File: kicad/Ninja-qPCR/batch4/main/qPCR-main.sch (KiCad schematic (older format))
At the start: 39 parts, among them J1 Raspberry_Pi_3A_Plus_wpi, J2 Conn_01x03_Male, J3 Conn_01x01_Male, J4 Conn_01x01_Male, J5 Conn_02x03_Odd_Even, J6 Conn_02x03_Odd_Even, J7 Conn_02x03_Odd_Even, Q1 Q_NMOS_GSD, Q2 Q_NMOS_GSD, Q3 Q_NMOS_GSD, Q4 Q_NMOS_GSD, Q5 Q_NMOS_GSD, Q6 Q_NMOS_GSD, SW1 TACTILE_4

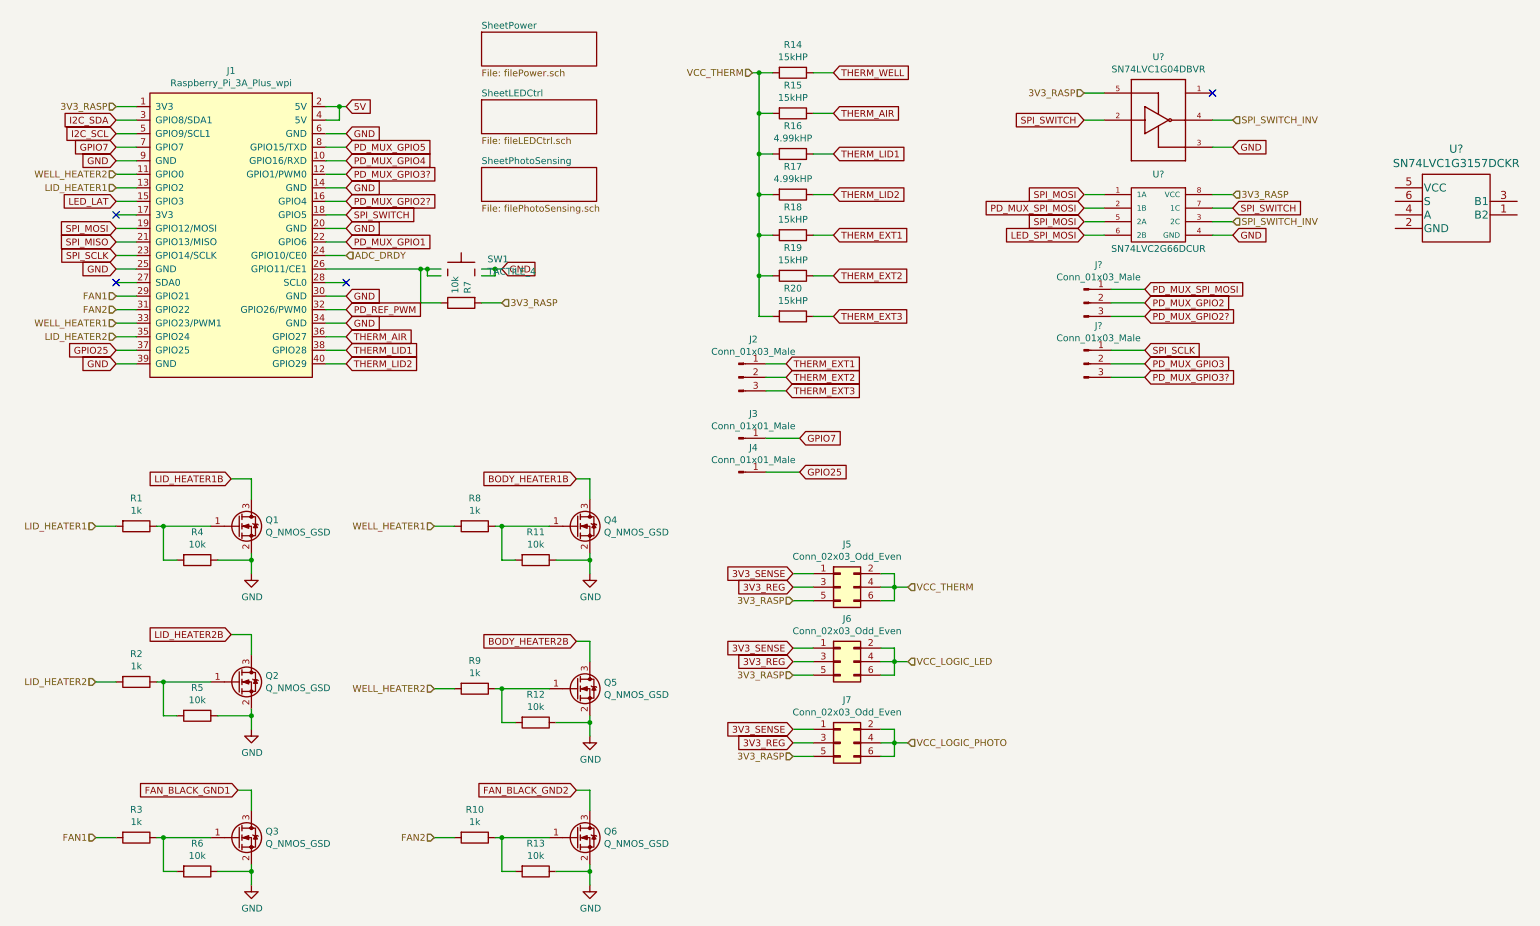
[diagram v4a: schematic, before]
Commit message: add gg component yaml
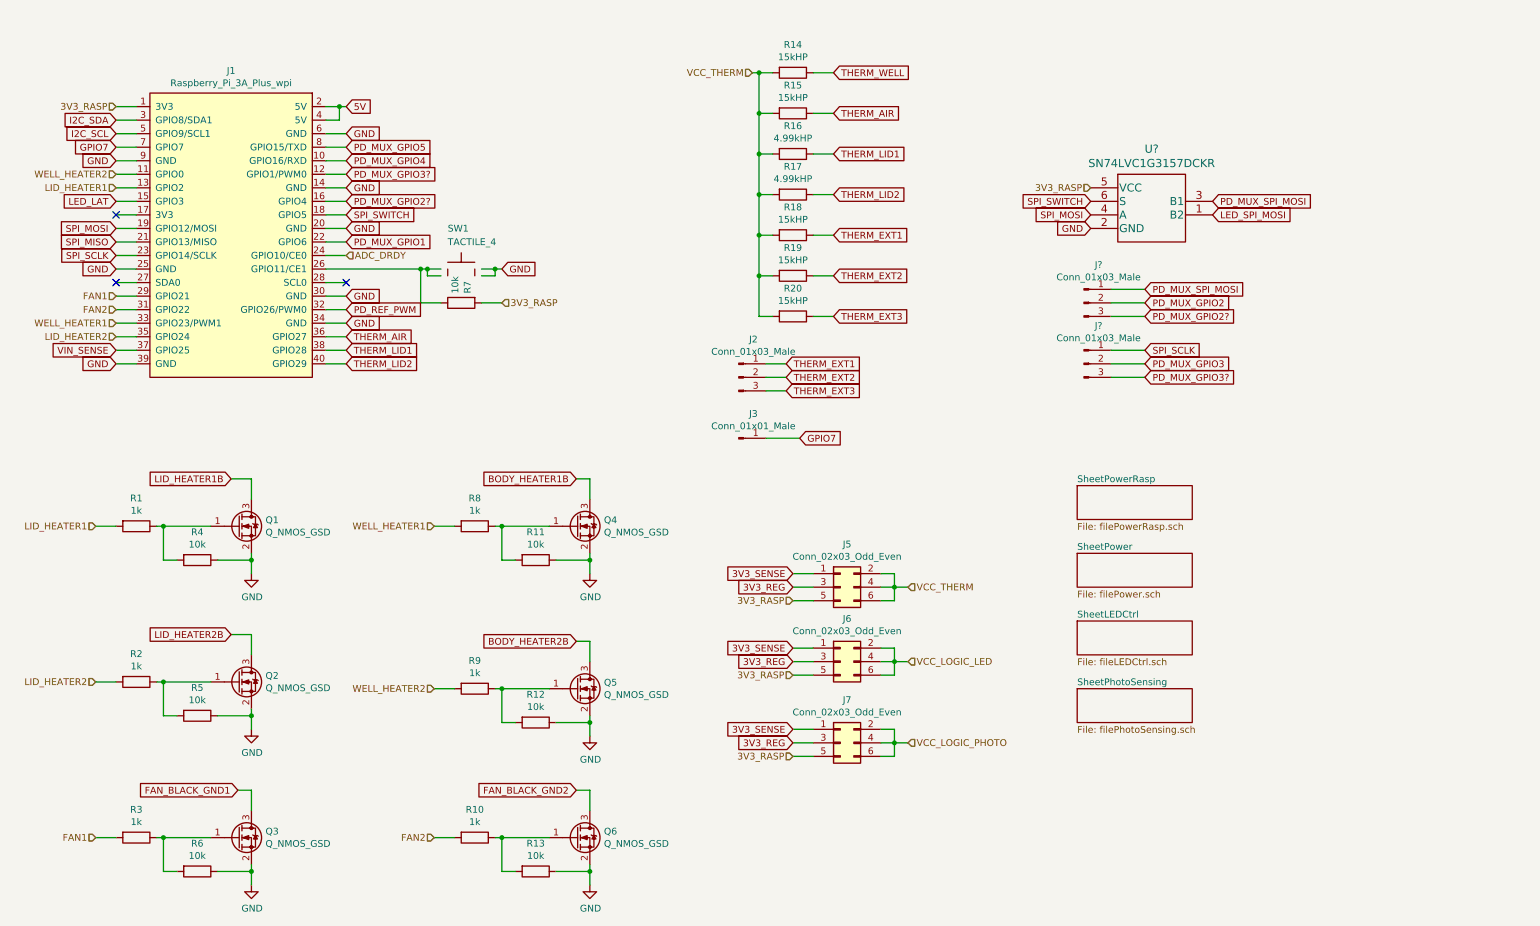
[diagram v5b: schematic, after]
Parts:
- removed J4: Conn_01x01_Male, Pin_Headers:Pin_Header_Straight_1x01_Pitch2.54mm, symbol Connector:Conn_01x01_Male
- removed U?: SN74LVC1G04DBVR, Ninja-qPCR:SN74LVC1G04DBVR, symbol Ninja-qPCR:SN74LVC1G04DBVR
- removed U?: SN74LVC2G66DCUR, Ninja-qPCR:SN74LVC2G66DCUR, symbol Ninja-qPCR:SN74LVC2G66DCUR
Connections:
- net 3V3_RASP: now also U?.5 (VCC)
- net GND: now also U?.2 (GND)
- net LED_SPI_MOSI: now also U?.1 (B2)
- net PD_MUX_SPI_MOSI: now also U?.3 (B1)
- net SPI_MOSI: now also U?.4 (A)
- net SPI_SWITCH: now also U?.6 (S)
- net GPIO25 renamed VIN_SENSE
- no-connect marks 4 -> 3
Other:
- moved on the sheet: U?
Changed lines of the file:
@@
 $Descr A4 11693 8268
 encoding utf-8
-Sheet 1 4
+Sheet 1 5
 Title ""
 Date ""
@@
 Wire Wire Line
 	3700 2950 3550 2950
-Text GLabel 2000 3250 0    50   Input ~ 0
-GPIO25
 Wire Wire Line
 	2000 3250 2150 3250
@@
 	4850 2900 4700 2900
 Wire Wire Line
-	4850 2650 4800 2650
-Text GLabel 4850 2650 2    50   Input ~ 0
-GND
-Wire Wire Line
 	4300 2700 4300 2650
 Connection ~ 4300 2650
@@
 Connection ~ 4800 2650
 $Sheet
-S 4700 900  850  250
+S 9100 4750 850  250
 U 5F7093B5
 F0 "SheetPower" 50
@@
 Text GLabel 7050 3900 2    50   Input ~ 0
 GPIO7
-Text GLabel 7050 4150 2    50   Input ~ 0
-GPIO25
 Wire Wire Line
 	7050 3900 6800 3900
-Wire Wire Line
-	7050 4150 6800 4150
 NoConn ~ 2000 2250
 Wire Wire Line
@@
 Wire Wire Line
 	9600 3450 9350 3450
-Text GLabel 9150 1550 0    50   Input ~ 0
-SPI_SWITCH
-NoConn ~ 10100 1350
-Text HLabel 10250 1550 2    50   Input ~ 0
-SPI_SWITCH_INV
-Text GLabel 10250 1750 2    50   Input ~ 0
-GND
-Wire Wire Line
-	10250 1750 10100 1750
-Wire Wire Line
-	10250 1550 10100 1550
-Wire Wire Line
-	9300 1350 9150 1350
-Wire Wire Line
-	9300 1550 9150 1550
-Text HLabel 9150 1350 0    50   Input ~ 0
-3V3_RASP
-$Comp
-L Ninja-qPCR:SN74LVC1G04DBVR U?
-U 1 1 602B5E4F
-P 9700 1550
-AR Path="/602B5E4F" Ref="U?"  Part="1"
-AR Path="/5FA5D98E/602B5E4F" Ref="U?"  Part="1"
-F 0 "U?" H 9700 2017 50  0000 C CNN
-F 1 "SN74LVC1G04DBVR" H 9700 1926 50  0000 C CNN
-F 2 "Ninja-qPCR:SN74LVC1G04DBVR" H 9700 1550 50  0001 L BNN
-F 3 "IPC-7351B" H 9700 1550 50  0001 L BNN
-F 4 "1.45mm" H 9700 1550 50  0001 L BNN "Field4"
-F 5 "AD" H 9700 1550 50  0001 L BNN "Field5"
-F 6 "Texas Instruments" H 9700 1550 50  0001 L BNN "Field6"
-	1    9700 1550
-	1    0    0    -1
-$EndComp
 $Comp
 L Connector:Conn_01x03_Male J?
@@
 F 3 "~" H 9150 2900 50  0001 C CNN
 	1    9150 2900
-	1    0    0    -1
-$EndComp
-$Comp
-L Ninja-qPCR:TACTILE_4 SW1
-U 1 1 5F67E494
-P 4550 2650
-F 0 "SW1" H 4744 2723 50  0000 L CNN
-F 1 "TACTILE_4" H 4744 2632 50  0000 L CNN
-F 2 "Ninja-qPCR:SW_TH_Tactile_Omron_B3F-10xx" H 4550 2850 50  0001 C CNN
-F 3 "http://www.apem.com/int/index.php?controller=attachment&id_attachment=488" H 4550 2850 50  0001 C CNN
-	1    4550 2650
 	1    0    0    -1
 $EndComp
@@
 $EndComp
 $Comp
-L Connector:Conn_01x01_Male J4
-U 1 1 5F920692
-P 6600 4150
-F 0 "J4" H 6708 4331 50  0000 C CNN
-F 1 "Conn_01x01_Male" H 6708 4240 50  0000 C CNN
-F 2 "Pin_Headers:Pin_Header_Straight_1x01_Pitch2.54mm" H 6600 4150 50  0001 C CNN
-F 3 "~" H 6600 4150 50  0001 C CNN
-	1    6600 4150
-	1    0    0    -1
-$EndComp
-$Comp
 L Connector:Conn_01x01_Male J3
 U 1 1 5F91FDBE
@@
 	1    0    0    -1
 $EndComp
-$Comp
-L Ninja-qPCR:SN74LVC2G66DCUR U?
-U 1 1 602B5E5D
-P 9500 2100
-AR Path="/602B5E5D" Ref="U?"  Part="1"
-AR Path="/5FA5D98E/602B5E5D" Ref="U?"  Part="1"
-F 0 "U?" H 9700 2250 50  0000 C CNN
-F 1 "SN74LVC2G66DCUR" H 9700 1700 50  0000 C CNN
-F 2 "Ninja-qPCR:SN74LVC2G66DCUR" H 9500 2100 50  0001 L BNN
-F 3 "" H 9500 2100 50  0001 C CNN
-	1    9500 2100
-	1    0    0    -1
-$EndComp
-Text HLabel 10250 2100 2    50   Input ~ 0
+Text HLabel 9200 2050 0    50   Input ~ 0
 3V3_RASP
-Wire Wire Line
-	9300 2400 9150 2400
-Wire Wire Line
-	9300 2300 9150 2300
-Wire Wire Line
-	9300 2200 9150 2200
-Wire Wire Line
-	9300 2100 9150 2100
-Wire Wire Line
-	10100 2300 10250 2300
-Wire Wire Line
-	10100 2200 10250 2200
-Wire Wire Line
-	10250 2100 10100 2100
-Wire Wire Line
-	10250 2400 10100 2400
-Text GLabel 10250 2400 2    50   Input ~ 0
+Text GLabel 9200 2350 0    50   Input ~ 0
 GND
-Text GLabel 9150 2400 0    50   Input ~ 0
+Text GLabel 10100 2250 2    50   Input ~ 0
 LED_SPI_MOSI
-Text GLabel 9150 2300 0    50   Input ~ 0
+Text GLabel 10100 2150 2    50   Input ~ 0
+PD_MUX_SPI_MOSI
+Text GLabel 9200 2250 0    50   Input ~ 0
 SPI_MOSI
-Text GLabel 9150 2200 0    50   Input ~ 0
-PD_MUX_SPI_MOSI
-Text GLabel 9150 2100 0    50   Input ~ 0
-SPI_MOSI
-Text HLabel 10250 2300 2    50   Input ~ 0
-SPI_SWITCH_INV
-Text GLabel 10250 2200 2    50   Input ~ 0
-SPI_SWITCH
 $Sheet
-S 4700 1400 850  250
+S 9100 5250 850  250
 U 603C63DB
 F0 "SheetLEDCtrl" 50
@@
 $EndSheet
 $Sheet
-S 4700 1900 850  250
+S 9100 5750 850  250
 U 603C6849
 F0 "SheetPhotoSensing" 50
@@
 L Ninja-qPCR:SN74LVC1G3157DCKR U?
 U 1 1 602E131D
-P 11450 2050
-F 0 "U?" H 11900 2337 60  0000 C CNN
-F 1 "SN74LVC1G3157DCKR" H 11900 2231 60  0000 C CNN
-F 2 "DCK0006A_N" H 11900 1450 60  0001 C CNN
-F 3 "" H 12350 1750 60  0000 C CNN
-	1    11450 2050
-	1    0    0    -1
-$EndComp
+P 9200 2050
+F 0 "U?" H 9650 2337 60  0000 C CNN
+F 1 "SN74LVC1G3157DCKR" H 9650 2231 60  0000 C CNN
+F 2 "DCK0006A_N" H 9650 1450 60  0001 C CNN
+F 3 "" H 10100 1750 60  0000 C CNN
+	1    9200 2050
+	1    0    0    -1
+$EndComp
+Text GLabel 9200 2150 0    50   Input ~ 0
+SPI_SWITCH
+$Sheet
+S 9100 4250 850  250
+U 602F5E03
+F0 "SheetPowerRasp" 50
+F1 "filePowerRasp.sch" 50
+$EndSheet
+Text GLabel 2000 3250 0    50   Input ~ 0
+VIN_SENSE
+$Comp
+L Ninja-qPCR:TACTILE_4 SW1
+U 1 1 5F67E494
+P 4550 2650
+F 0 "SW1" H 4450 2950 50  0000 L CNN
+F 1 "TACTILE_4" H 4450 2850 50  0000 L CNN
+F 2 "Ninja-qPCR:SW_TH_Tactile_Omron_B3F-10xx" H 4550 2850 50  0001 C CNN
+F 3 "http://www.apem.com/int/index.php?controller=attachment&id_attachment=488" H 4550 2850 50  0001 C CNN
+	1    4550 2650
+	1    0    0    -1
+$EndComp
+Wire Wire Line
+	4850 2650 4800 2650
+Text GLabel 4850 2650 2    50   Input ~ 0
+GND
 $EndSCHEMATC
